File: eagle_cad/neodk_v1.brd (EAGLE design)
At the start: 80 x 41 mm, 73 parts, among them J1 SWD, J2 Power 5V..12V DC, J3 FC68131, J4 S2B-XH-A(LF)(SN), J5 S2B-XH-A(LF)(SN), Q1 IRLML6344TRPBF, Q2 IRLML6344TRPBF, Q3 PMV50EPEAR, SW2 FSMRA6JH, U1 SGM61410XN6G/TR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

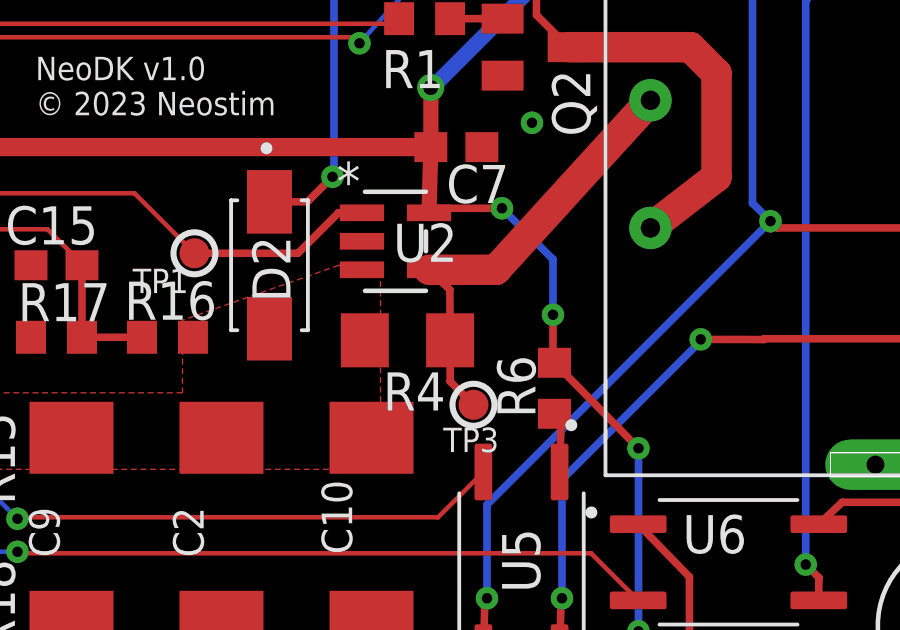
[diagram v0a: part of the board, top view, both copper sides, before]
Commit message: Prep for serial comms and pulse sequencer.
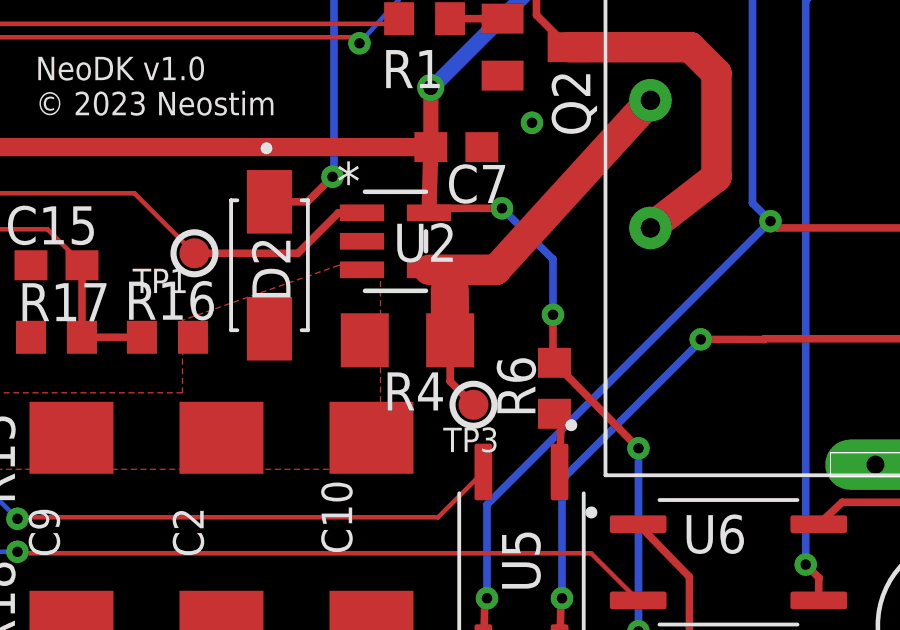
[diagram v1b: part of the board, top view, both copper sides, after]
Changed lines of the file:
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@@
 <contactref element="R4" pad="1"/>
 <wire x1="47.1176" y1="14.85" x2="47.812" y2="14.1856" width="0.254" layer="1"/>
-<wire x1="47.812" y1="14.1856" x2="47.822" y2="12.5" width="0.254" layer="1"/>
+<wire x1="47.812" y1="14.1856" x2="47.822" y2="12.5" width="1.27" layer="1"/>
 <wire x1="47.1176" y1="14.85" x2="49.35" y2="14.85" width="1.016" layer="1"/>
 <wire x1="49.35" y1="14.85" x2="54.5" y2="20.5" width="1.016" layer="1"/>

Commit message: Updated schematic and board.
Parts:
- moved J3 0.54 mm to (4.00, 27.5)
- moved J2 0.20 mm to (-3.40, 14.6)
- moved SW2 0.10 mm to (77.3, 26.2)
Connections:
- net VCC: no longer D3.4
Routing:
- net VCC: track 172.4 -> 150.3 mm, vias 14 -> 12
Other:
- board text added: "NeoDK v1.1 © 2023, 2024 Neostim"
- board text removed: "NeoDK v1.0 © 2023 Neostim"
